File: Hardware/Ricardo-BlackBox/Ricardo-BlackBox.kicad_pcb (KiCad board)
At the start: 4 copper layers, 80.3 x 54.1 mm, 87 parts, among them IC1 XTSD08GLGEAG, IC2 CP2102N-A02-GQFN24, J1 RBUS, J2 USB_C_Receptacle_USB2.0, U1 ESP32-S3, U2 SN65HVD230, U3 LM66200DRLR, U4 MAX77827AEFD+T, U5 SC4215, Y1 40MHz±10ppm

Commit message: Initial hardware update
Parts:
- removed C19: 220pF, Capacitor_SMD:C_0402_1005Metric
- removed C28: 10uF, Capacitor_SMD:C_0402_1005Metric
- removed IC1: XTSD08GLGEAG, iclr:SOTFL50P160X60-8N
- removed IC2: CP2102N-A02-GQFN24, iclr:QFN50P400X400X80-25N
- removed TP11, TP12, TP13, TP14, TP3: TestPoint, TestPoint:TestPoint_Pad_D1.0mm
- removed TP7: TestPoint, TestPoint:TestPoint_Pad_D1.5mm
- added CRXLED1: ORANGE_LED, Resistor_SMD:R_0402_1005Metric, F.Cu at (97.1, 53.3)
- added CTXLED1: GREEN_LED, Resistor_SMD:R_0402_1005Metric, F.Cu at (98.9, 53.3)
- added J3: Conn_02x04_Odd_Even, Connector_PinHeader_2.54mm:PinHeader_2x04_P2.54mm_Vertical, F.Cu at (123.0, 54.2)
- added J4: Conn_02x03_Odd_Even, Connector_PinHeader_2.54mm:PinHeader_2x03_P2.54mm_Vertical, F.Cu at (93.6, 60.5)
- added R20: 10K, Resistor_SMD:R_0402_1005Metric, F.Cu at (121.4, 60.4)
- added U6: XTSD08G, Package_LGA:LGA-8_8x6mm_P1.27mm, F.Cu at (117.6, 70.3)
- added U7: LM66200DRLR, iclr:SOTFL50P160X60-8N, F.Cu at (121.7, 63.6)
- added U8: SN74CBTLV3245APWR, SN74CBTLV3245APWR:SOP65P640X120-20N, F.Cu at (116.5, 62.8)
- 12VLED1: value 12V_LED -> RED_LED
- 3V3LED1: value 3V3LED -> BLUE_LED
- C12: value 4.2pF -> 10uF
- C13, C14: value C -> 11pF
- C17: value 0.1uF -> 47nF
- C18: value 220pF -> 0.1uF
- J2: footprint Connector_USB:USB_C_Receptacle_GCT_USB4085 -> Connector_USB:USB_C_Receptacle_Palconn_UTC16-G
- R10, R9: footprint Resistor_SMD:R_0402_1005Metric -> Resistor_SMD:R_0603_1608Metric
- R13: value 470 -> 5.1k
- R18: value 22.1k -> 1k
- R19: value 47.5k -> 10K
- R5: value 47.5 -> 1k
- R6: value 499 -> 499R
- TP10, TP9: moved to B.Cu
- TXLED1: value TX_LED -> GREEN_LED
- U1: footprint Package_DFN_QFN:QFN-56-1EP_7x7mm_P0.4mm_EP5.6x5.6mm -> iclr:QFN40P700X700X90-57N
- U5: value SC4215 -> SC4215ASTRT
- USBLED1: value USB_LED -> WHITE_LED
- Y1: value 40MHz±10ppm -> R940000171
- moved H4 64.4 mm to (82.9, 77.6)
- moved H3 43.4 mm to (121.9, 77.6)
- moved TXLED1 42.6 mm to (111.7, 53.5), turned to 180 degrees
- moved TP9 41.1 mm to (112.9, 55.7), turned to 180 degrees
- moved H2 40.7 mm to (121.9, 49.1)
- moved TP6 39.0 mm to (89.7, 78.9)
- moved J2 38.5 mm to (107.4, 76.3), turned to 0 degrees
- moved R9 35.8 mm to (92.5, 51.3)
- moved TP8 34.9 mm to (93.4, 68.7)
- moved TP4 34.6 mm to (87.8, 69.5)
- moved R19 33.8 mm to (121.4, 61.4), turned to 180 degrees
- moved BOOTJUMPER1 33.4 mm to (113.0, 49.4), turned to 90 degrees
- moved C8 33.2 mm to (117.9, 48.4), turned to 90 degrees
- moved R4 32.9 mm to (83.4, 72.6)
- moved C21 32.7 mm to (90.1, 74.7)
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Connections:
- C12 pad 1: Net-(C12-Pad1) -> /NAND_3V3
- C12 pad 2: Net-(C12-Pad2) -> GND
- C18 pad 1: GND -> /NAND_3V3
- C18 pad 2: /CAN+ -> GND
- D2 pad 2: Net-(D2-Pad2) -> /Data+
- D2 pad 3: Net-(D2-Pad3) -> /Data-
- D2 pad 4: Net-(D2-Pad4) -> VBUS
- J2 pad A4: Net-(D2-Pad2) -> VBUS
- J2 pad A6: Net-(D2-Pad3) -> /Data+
- J2 pad A7: Net-(D2-Pad4) -> /Data-
- J2 pad A9: Net-(D2-Pad2) -> VBUS
- J2 pad B4: Net-(D2-Pad2) -> VBUS
- J2 pad B6: Net-(D2-Pad3) -> /Data+
- J2 pad B7: Net-(D2-Pad4) -> /Data-
- J2 pad B9: Net-(D2-Pad2) -> VBUS
- R18 pad 1: Net-(D2-Pad2) -> +3V3
- R18 pad 2: Net-(IC2-Pad8) -> Net-(CRXLED1-A)
- R19 pad 1: Net-(IC2-Pad8) -> Net-(U7-ST)
- R19 pad 2: GND -> +3V3
- R5 pad 1: GND -> +3V3
- R5 pad 2: Net-(C12-Pad1) -> Net-(CTXLED1-A)
- R6 pad 1: /RXD -> /TXD
- U1 pad 1: Net-(C12-Pad2) -> unconnected-(U1-LNA_IN/RF-Pad1)
- U1 pad 10: unconnected-(U1-Pad10) -> /GPIO_5
- U1 pad 11: unconnected-(U1-Pad11) -> /GPIO_6
- U1 pad 12: unconnected-(U1-Pad12) -> /GPIO_7
- U1 pad 37: unconnected-(U1-Pad37) -> /NAND_SD2
- U1 pad 38: unconnected-(U1-Pad38) -> /NAND_SD3
- U1 pad 39: unconnected-(U1-Pad39) -> /NAND_CLK
- U1 pad 40: /NAND_CS -> /NAND_CMD
- U1 pad 41: /CLK -> /NAND_SD0
- U1 pad 42: /MISO -> /NAND_SD1
- U1 pad 43: /MOSI -> unconnected-(U1-GPIO38-Pad43)
- U1 pad 50: /TXD -> /RXD
- U1 pad 6: unconnected-(U1-Pad6) -> /CAN_TX
- U1 pad 7: unconnected-(U1-Pad7) -> /CAN_RX
- U1 pad 9: unconnected-(U1-Pad9) -> /GPIO_4
- U5 pad 5: (no net) -> unconnected-(U5-NC-Pad5)
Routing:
- net +3V3: track 1.61 -> 37.6 mm, vias 1 -> 16
- net VBUS: track 5.27 -> 39.7 mm, vias 2 -> 4
- net /BOOT: track 0.00 -> 32.8 mm, vias 0 -> 1
- net /CAN+: track 0.00 -> 30.0 mm
- net /CAN-: track 0.00 -> 29.8 mm
- net RBUS_uC_V: track 0.00 -> 26.3 mm
- net /CAN_RX: track 0.00 -> 24.6 mm
- net /Data-: track 0.00 -> 22.9 mm
- net /CHIP_PU: track 0.00 -> 22.4 mm, vias 0 -> 1
- net /Data+: track 0.00 -> 21.5 mm
- net /CAN_TX: track 0.00 -> 20.0 mm
- net /NAND_CMD: track 0.00 -> 18.3 mm
- net /NAND_SD0: track 0.00 -> 17.6 mm
- net /NAND_SD1: track 0.00 -> 17.0 mm
- net /NAND_CLK: track 0.00 -> 14.7 mm
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- added copper zone on In2.Cu, net +3V3
- added copper zone on B.Cu, net GND
- added copper zone on In1.Cu, net GND
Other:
- board size 80.3 x 54.1 mm -> 45.8 x 35.1 mm
- board text added: "BlackBox"
- board text added: "by maxhlc"

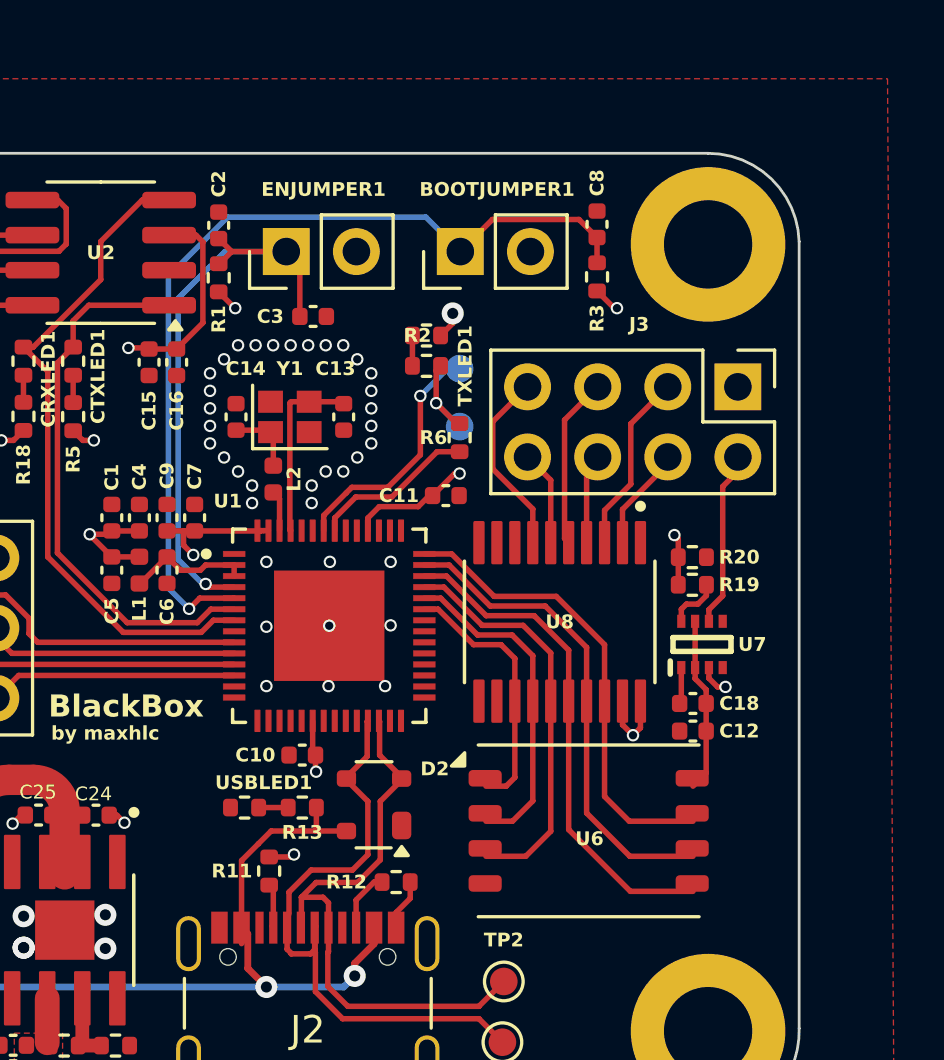
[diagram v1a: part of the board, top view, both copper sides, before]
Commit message: Moved decoupling capacitors
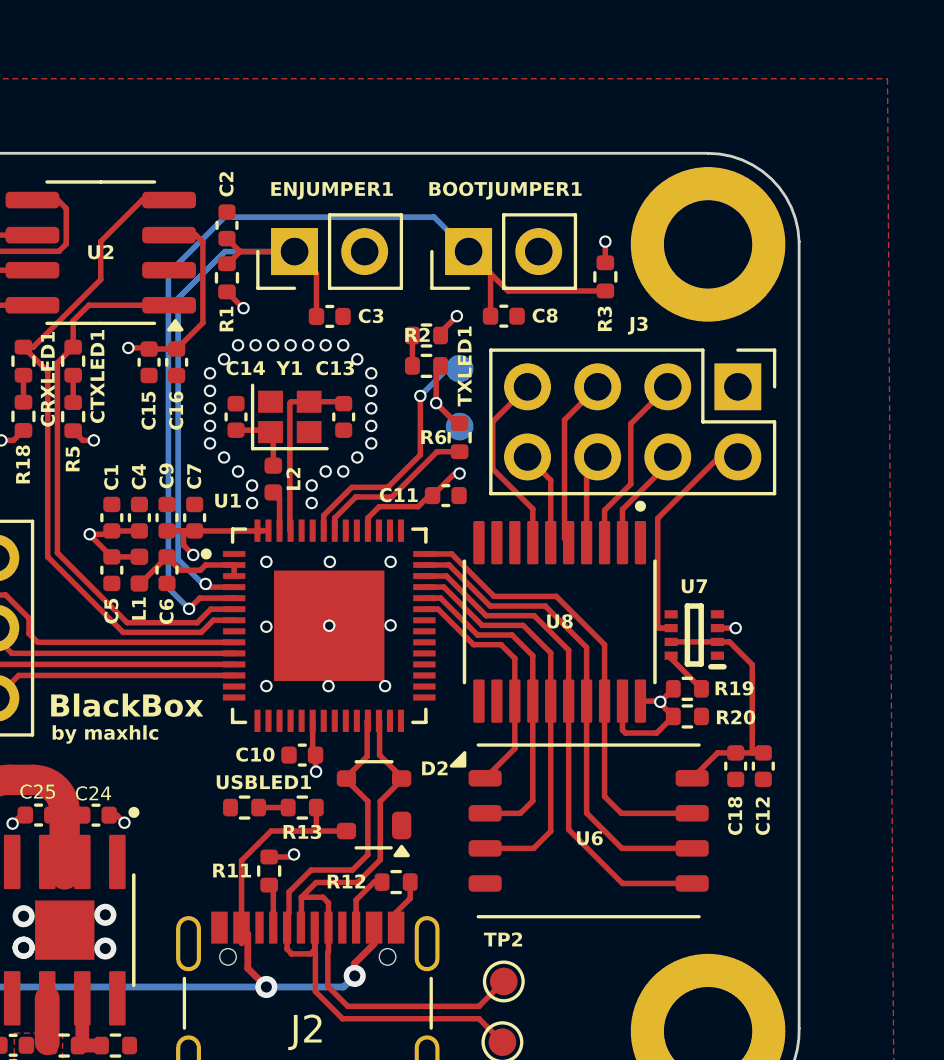
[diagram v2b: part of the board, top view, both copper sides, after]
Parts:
- moved R20 5.77 mm to (121.2, 66.2), turned to 180 degrees
- moved C8 4.74 mm to (114.5, 51.7), turned to 0 degrees
- moved R19 3.77 mm to (121.2, 65.2)
- moved C12 2.85 mm to (123.9, 68.0), turned to -90 degrees
- moved C18 2.75 mm to (122.9, 68.0), turned to -90 degrees
- moved C3 0.60 mm to (108.2, 51.7)
- moved U7 0.44 mm to (121.4, 63.2), turned to 180 degrees
- moved BOOTJUMPER1 0.30 mm to (113.2, 49.4)
- moved C2 0.30 mm to (104.5, 48.4)
- moved ENJUMPER1 0.30 mm to (106.9, 49.4)
- moved R1 0.30 mm to (104.5, 50.3)
- moved R3 0.30 mm to (118.2, 50.3), turned to -90 degrees
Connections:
- R20 pad 1: +3V3 -> GND
- R20 pad 2: GND -> +3V3
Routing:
- net /NAND_3V3: track 6.33 -> 9.43 mm
- net /HEADER_3V3: track 6.39 -> 9.11 mm
- net /BOOT: track 32.8 -> 34.7 mm
- net GND: track 13.9 -> 12.5 mm
- net /NAND_SD2: track 9.51 -> 8.80 mm
- net +3V3: track 37.6 -> 37.8 mm, vias 16 -> 15

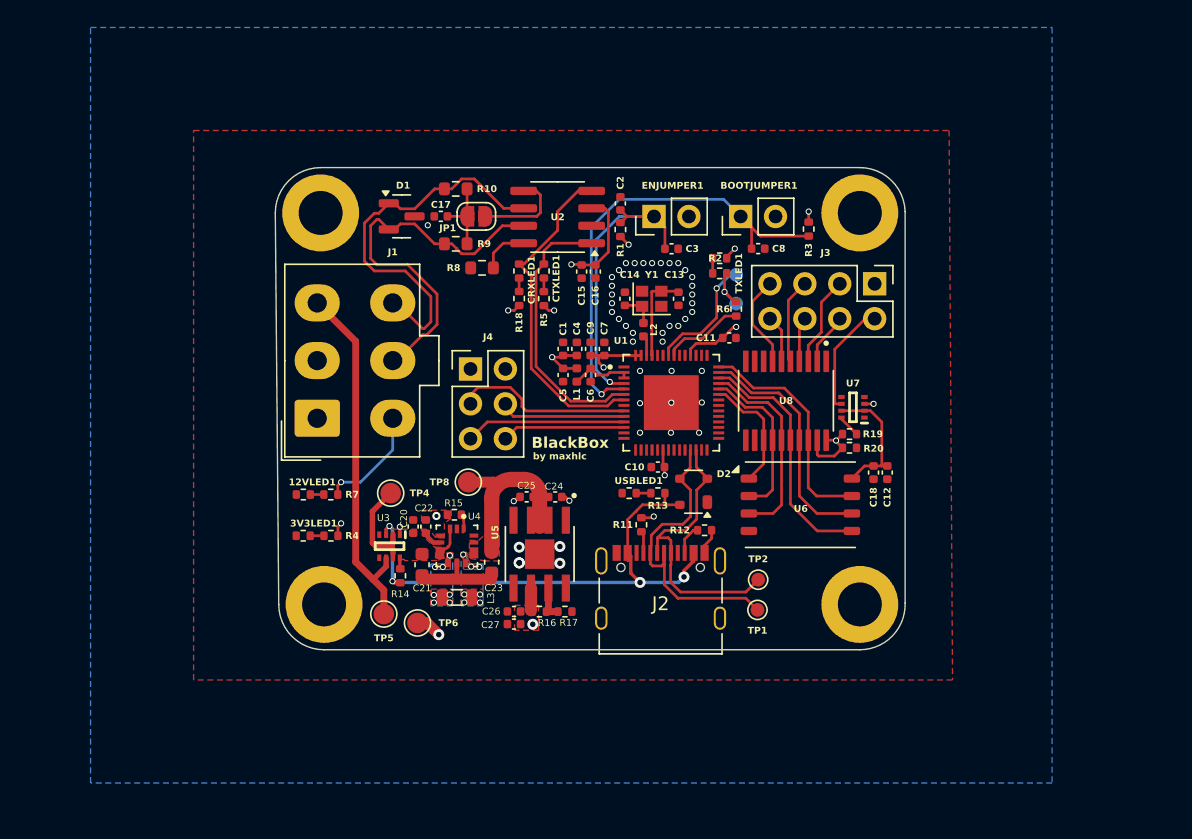
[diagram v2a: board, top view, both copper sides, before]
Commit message: Moved USB test pads
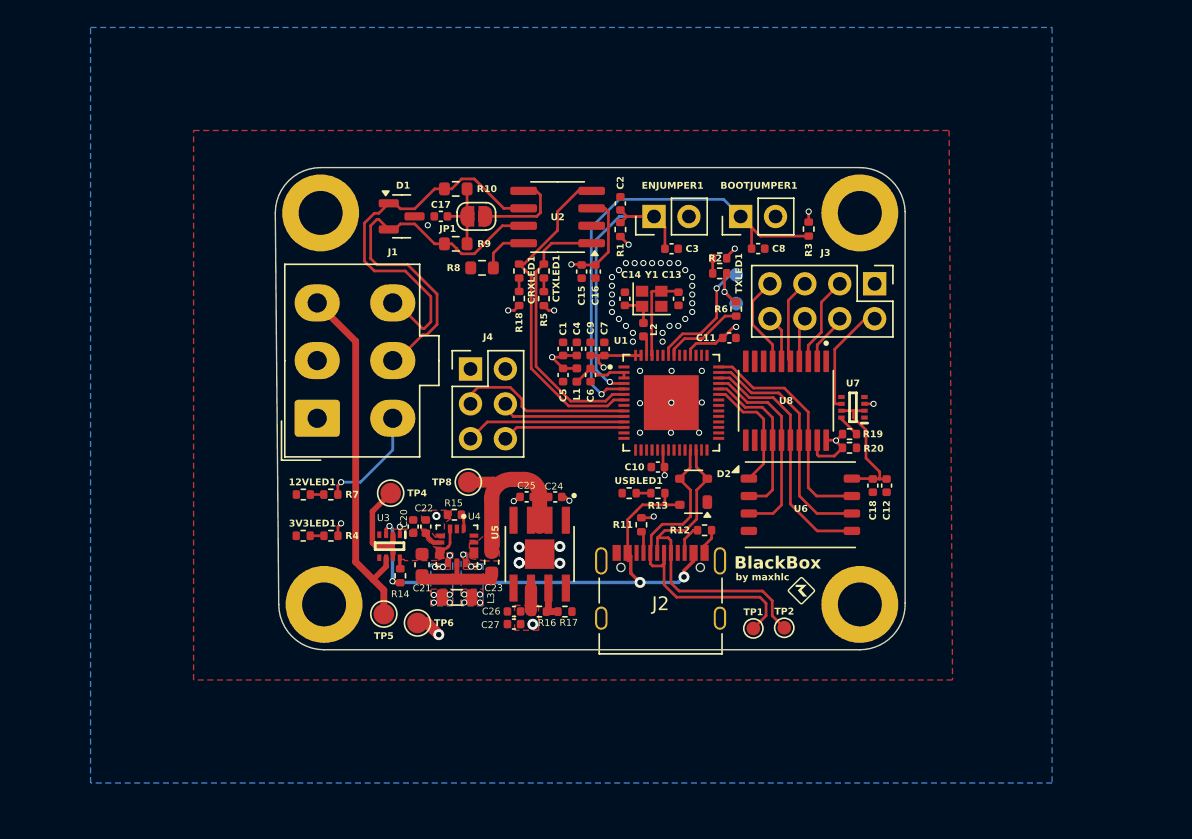
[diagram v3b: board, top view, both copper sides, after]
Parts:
- added G***: LOGO, iclr:rae_logo_2mm, F.Cu at (117.7, 76.6)
- moved TP2 3.98 mm to (116.4, 79.3)
- moved TP1 1.38 mm to (114.2, 79.3)
- moved C12 0.95 mm to (123.9, 68.9)
- moved C18 0.95 mm to (122.9, 68.9)
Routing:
- net /Data+: track 21.5 -> 24.7 mm
- net /Data-: track 22.9 -> 25.5 mm
- net /NAND_3V3: track 9.43 -> 9.97 mm

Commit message: Removed data line switching and rearranged
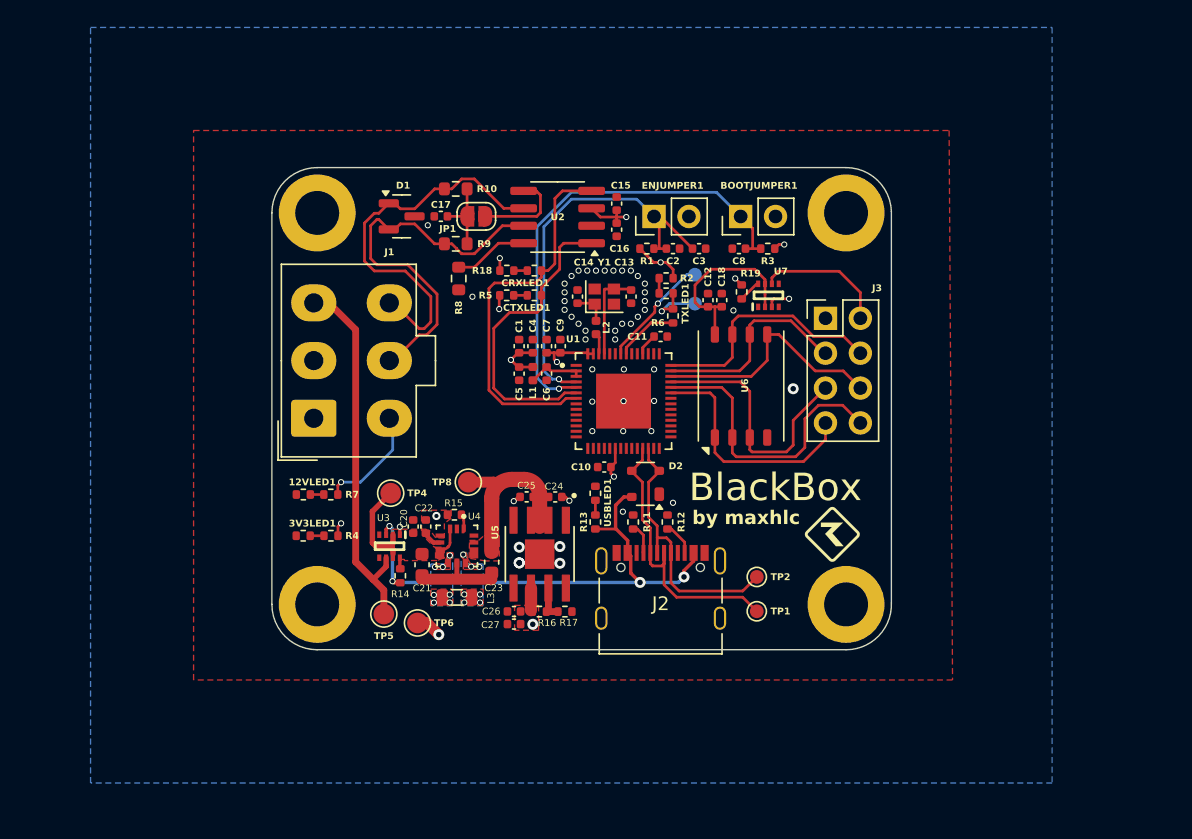
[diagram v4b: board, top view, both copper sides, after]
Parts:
- removed the G*** at (117.7, 76.6)
- removed J4: Conn_02x03_Odd_Even, Connector_PinHeader_2.54mm:PinHeader_2x03_P2.54mm_Vertical
- removed R20: 10K, Resistor_SMD:R_0402_1005Metric
- removed U8: SN74CBTLV3245APWR, SN74CBTLV3245APWR:SOP65P640X120-20N
- added G***: LOGO, iclr:rae_logo_4mm, F.Cu at (119.9, 72.5)
- moved C12 18.7 mm to (110.9, 55.4), turned to 90 degrees
- moved C18 17.4 mm to (111.9, 55.4), turned to 90 degrees
- moved R19 13.0 mm to (113.3, 54.8), turned to 90 degrees
- moved U7 10.2 mm to (115.3, 55.1), turned to 90 degrees
- moved U6 9.66 mm to (113.3, 61.7), turned to 90 degrees
- moved C15 5.57 mm to (104.2, 48.4), turned to 90 degrees
- moved C2 5.05 mm to (108.3, 51.7), turned to 0 degrees
- moved R13 5.01 mm to (102.7, 71.6), turned to 90 degrees
- moved C11 5.00 mm to (107.4, 58.1)
- moved R6 4.63 mm to (108.3, 56.6)
- moved J3 4.37 mm to (119.4, 56.8), turned to 0 degrees
- moved TP2 4.21 mm to (114.4, 75.6)
- moved C7 4.20 mm to (99.1, 58.8)
- moved R2 4.16 mm to (107.8, 53.8)
- moved TXLED1 4.16 mm to (107.8, 54.9)
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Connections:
- J3 pad 3: /HEADER_SD0 -> /NAND_SD0
- J3 pad 4: /HEADER_SD1 -> /NAND_SD1
- J3 pad 5: /HEADER_CLK -> /NAND_CLK
- J3 pad 6: /HEADER_CMD -> /NAND_CMD
- J3 pad 7: /HEADER_SD2 -> /NAND_SD2
- J3 pad 8: /HEADER_SD3 -> /NAND_SD3
- U1 pad 10: /GPIO_5 -> unconnected-(U1-GPIO5/ADC1_CH4-Pad10)
- U1 pad 11: /GPIO_6 -> unconnected-(U1-GPIO6/ADC1_CH5-Pad11)
- U1 pad 12: /GPIO_7 -> unconnected-(U1-GPIO7/ADC1_CH6-Pad12)
- U1 pad 9: /GPIO_4 -> unconnected-(U1-GPIO4/ADC1_CH3-Pad9)
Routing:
- net /GPIO_4: track 13.1 -> 0.00 mm
- net /GPIO_6: track 11.7 -> 0.00 mm
- net /NAND_SD3: track 12.0 -> 21.5 mm
- net /GPIO_5: track 9.21 -> 0.00 mm
- net /GPIO_7: track 8.97 -> 0.00 mm
- net /NAND_SD2: track 8.80 -> 17.5 mm
- net +3V3: track 37.8 -> 29.2 mm, vias 15 -> 13
- net /CHIP_PU: track 22.9 -> 29.8 mm
- net /HEADER_SD2: track 6.80 -> 0.00 mm
- net /HEADER_SD0: track 6.59 -> 0.00 mm
- net /HEADER_CLK: track 6.20 -> 0.00 mm
- net /Data+: track 24.7 -> 20.2 mm
- net /NAND_CLK: track 14.7 -> 18.8 mm
- net /Data-: track 25.5 -> 21.7 mm
- net /HEADER_SD1: track 3.78 -> 0.00 mm
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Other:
- board size 45.8 x 35.1 mm -> 45.1 x 35.1 mm

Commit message: Fixed zone priorities
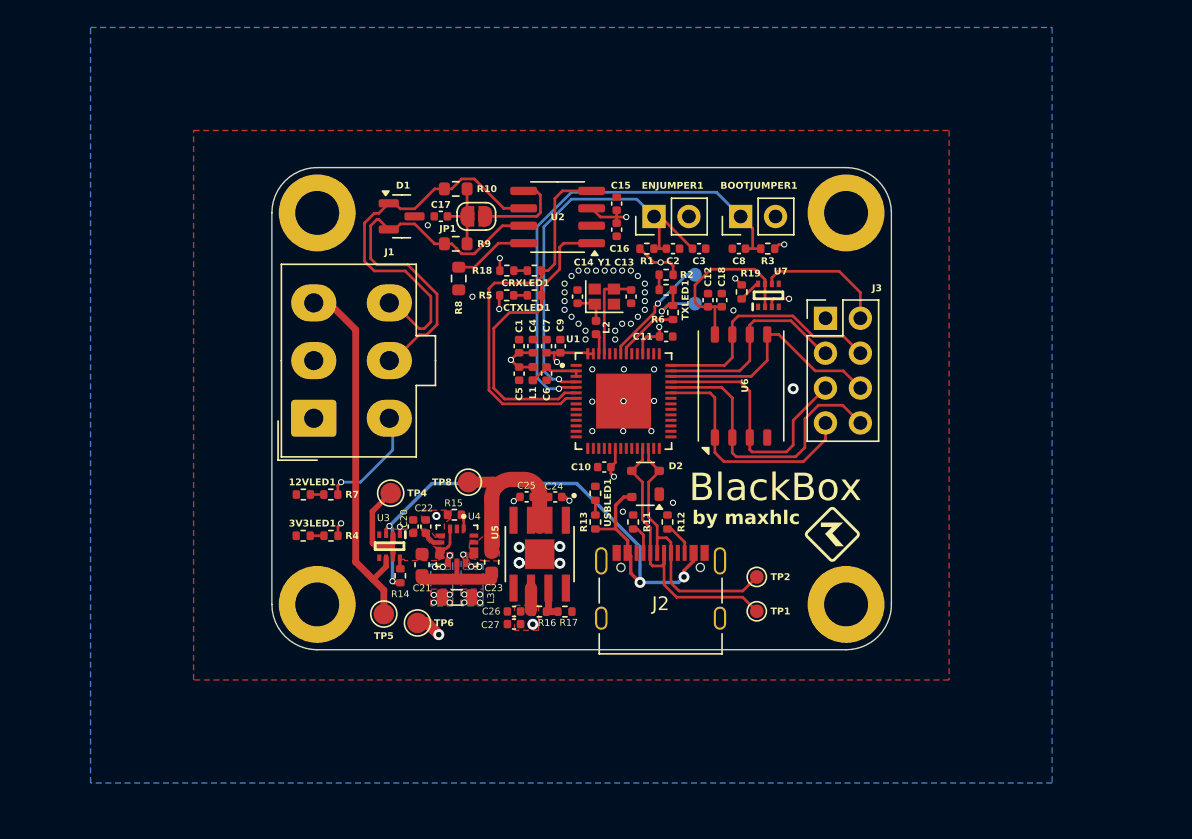
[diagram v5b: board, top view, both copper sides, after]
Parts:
- moved C11 0.40 mm to (107.8, 58.1)
- moved R2 0.25 mm to (107.8, 53.6)
- moved R6 0.25 mm to (108.3, 56.3)
- moved TXLED1 0.25 mm to (107.8, 54.7)
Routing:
- net VBUS: track 38.3 -> 44.3 mm
- net +3V3: track 29.2 -> 30.4 mm, vias 13 -> 14
